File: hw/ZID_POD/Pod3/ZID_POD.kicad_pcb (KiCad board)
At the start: 2 copper layers, 52.8 x 19.3 mm, 2 parts, among them J1 Z80-POD (3)

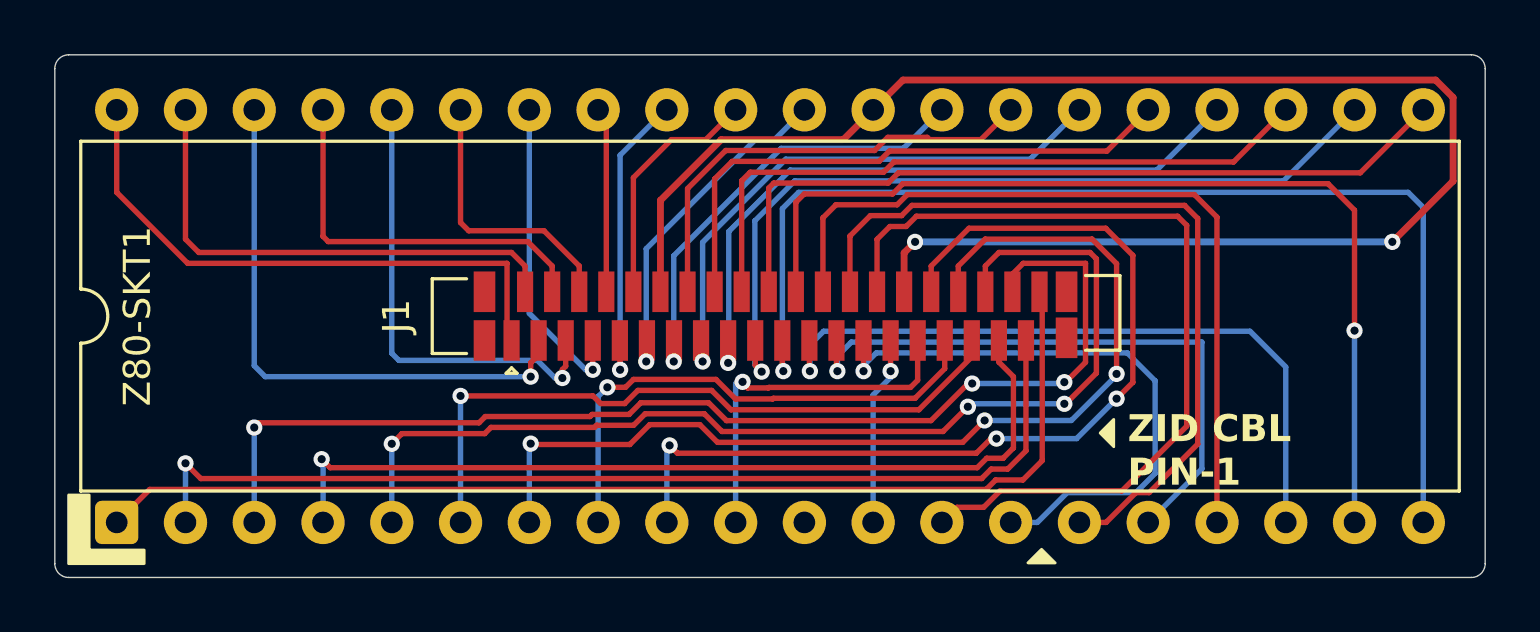
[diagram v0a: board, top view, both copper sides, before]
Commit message: PCB: Ready to order - ZID, POD1, POD2, POD3, POD4, ExpBP
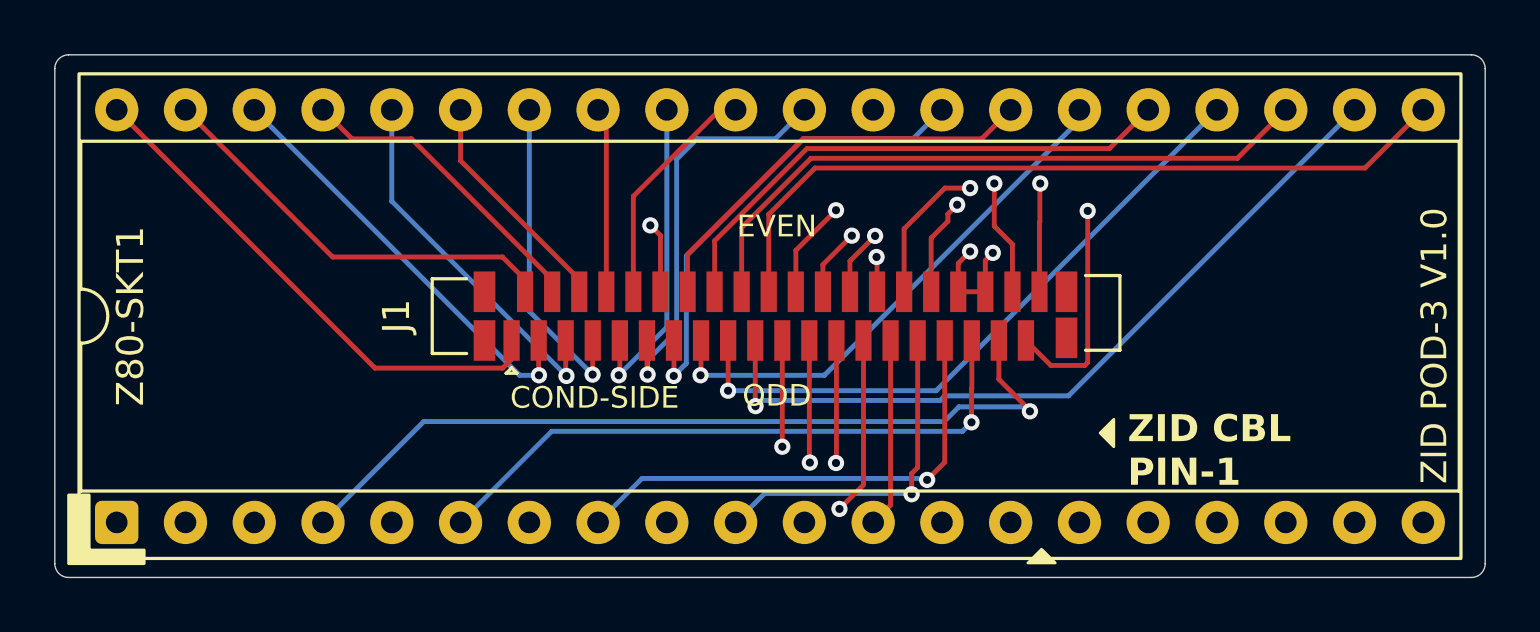
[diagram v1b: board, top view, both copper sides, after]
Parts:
- J1: value Z80-POD (3) -> FFC/FPC-40 Socket
- Z80-SKT1: footprint Package_DIP:DIP-40_W15.24mm -> Package_DIP:DIP-40_W15.24mm_Socket
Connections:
- J1 pad 12: /GND -> /A15
- J1 pad 30: /GND -> /D4
- J1 pad 34: /D4 -> /GND
- J1 pad 36: /A15 -> /GND
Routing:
- net /GND: track 60.7 -> 4.22 mm
- net /A15: track 40.1 -> 17.5 mm, vias 3 -> 1
- net /D7: track 31.8 -> 12.0 mm, vias 0 -> 1
- net /IORQ-: track 43.0 -> 29.1 mm
- net /D1: track 29.5 -> 16.2 mm, vias 0 -> 1
- net /D5: track 35.3 -> 24.5 mm, vias 3 -> 1
- net /A12: track 38.0 -> 47.9 mm
- net /MREQ-: track 36.2 -> 27.6 mm
- net /D0: track 22.2 -> 13.9 mm
- net /NMI-: track 29.3 -> 22.5 mm, vias 0 -> 1
- net /INT-: track 22.9 -> 17.2 mm
- net /A8: track 21.3 -> 15.9 mm
- net /A13: track 42.9 -> 38.2 mm, vias 3 -> 1
- net /D4: track 37.9 -> 33.3 mm, vias 3 -> 1
- net /A9: track 18.7 -> 15.1 mm
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- added copper zone on In1.Cu, net /GND
- added copper zone on In2.Cu, net /GND
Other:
- copper layers 2 -> 4
- board text added: "ZID POD-3 V1.0"
